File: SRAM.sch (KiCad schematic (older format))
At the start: 12 parts

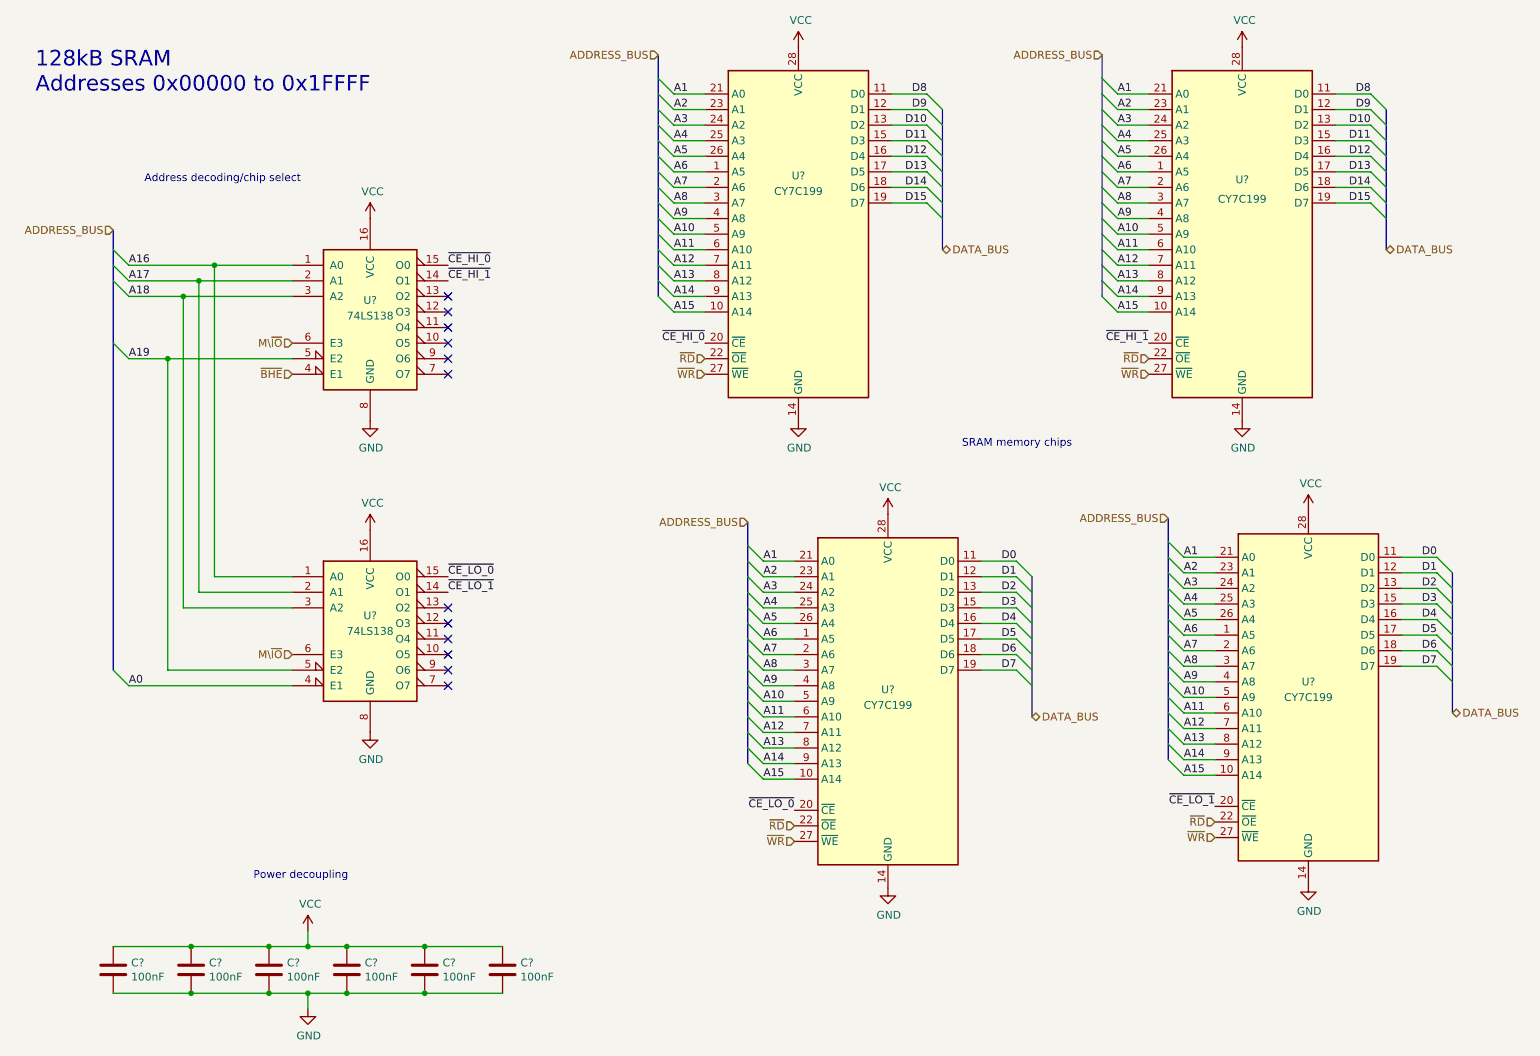
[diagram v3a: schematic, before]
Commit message: Updates to pass ERC
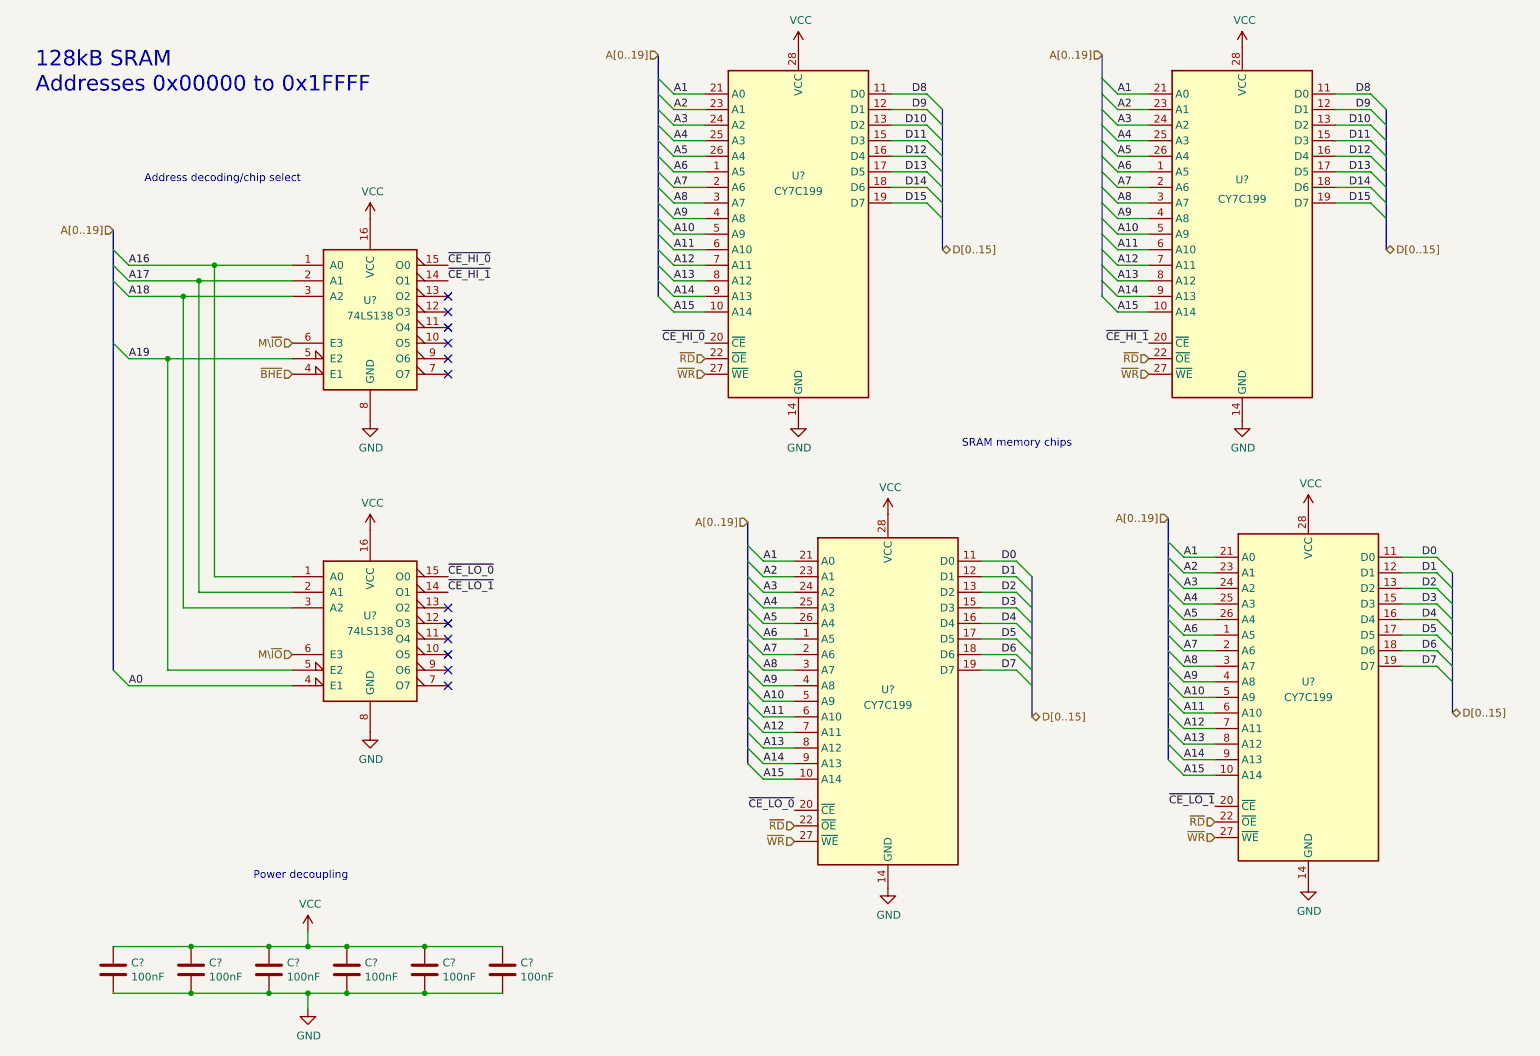
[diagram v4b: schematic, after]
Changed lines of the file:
@@
 	5050 1825 4850 1825
 Text HLabel 4750 875  0    50   Input ~ 0
-ADDRESS_BUS
+A[0..19]
 Wire Wire Line
 	7900 2525 7700 2525
@@
 	7900 1825 7700 1825
 Text HLabel 7600 875  0    50   Input ~ 0
-ADDRESS_BUS
+A[0..19]
 Wire Wire Line
 	5625 5525 5425 5525
@@
 	5625 4825 5425 4825
 Text HLabel 5325 3875 0    50   Input ~ 0
-ADDRESS_BUS
+A[0..19]
 Wire Wire Line
 	8325 5500 8125 5500
@@
 	8325 4800 8125 4800
 Text HLabel 8025 3850 0    50   Input ~ 0
-ADDRESS_BUS
+A[0..19]
 Entry Wire Line
 	7600 2425 7700 2525
@@
 $EndComp
 Text HLabel 1250 2000 0    50   Input ~ 0
-ADDRESS_BUS
+A[0..19]
 Entry Wire Line
 	1250 4825 1350 4925
@@
 	6575 1825 6475 1725
 Text HLabel 6575 2125 2    50   BiDi ~ 0
-DATA_BUS
+D[0..15]
 Wire Wire Line
 	9100 1825 9325 1825
@@
 	9425 1825 9325 1725
 Text HLabel 9425 2125 2    50   BiDi ~ 0
-DATA_BUS
+D[0..15]
 Wire Wire Line
 	9525 4800 9750 4800
@@
 	9850 4800 9750 4700
 Text HLabel 9850 5100 2    50   BiDi ~ 0
-DATA_BUS
+D[0..15]
 Wire Wire Line
 	6825 4825 7050 4825
@@
 	7150 4825 7050 4725
 Text HLabel 7150 5125 2    50   BiDi ~ 0
-DATA_BUS
+D[0..15]
 Wire Wire Line
 	1350 4925 2400 4925

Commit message: Assign footprints for most symbols
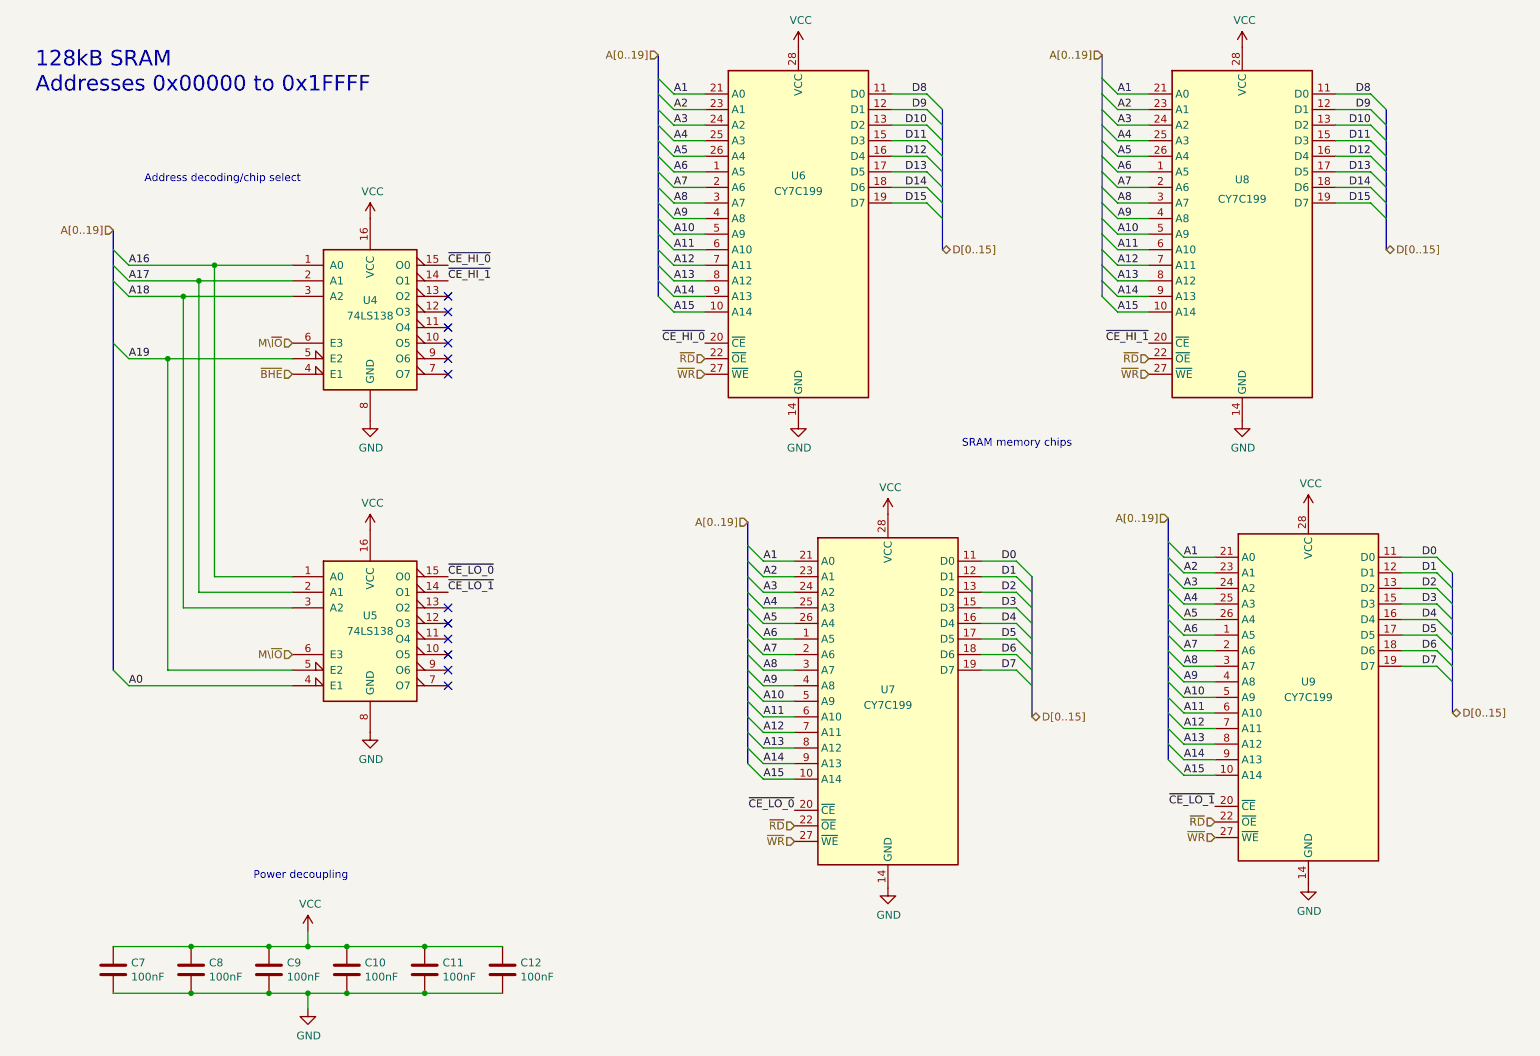
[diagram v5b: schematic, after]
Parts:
- C10, C11, C12, C7, C8, C9: renamed from C?; footprint (none) -> Capacitor_THT:C_Rect_L4.0mm_W2.5mm_P2.50mm
- U4, U5: renamed from U?; footprint (none) -> Package_DIP:DIP-16_W7.62mm
- U6, U7, U8, U9: renamed from U?; footprint (none) -> Package_DIP:DIP-28_W7.62mm
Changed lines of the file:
@@
 $EndDescr
 $Comp
-L Memory_RAM:CY7C199 U?
+L Memory_RAM:CY7C199 U6
 U 1 1 61AAD851
 P 5650 2025
-F 0 "U?" H 5650 2400 50  0000 C CNN
+F 0 "U6" H 5650 2400 50  0000 C CNN
 F 1 "CY7C199" H 5650 2300 50  0000 C CNN
-F 2 "" H 5650 2025 50  0001 C CNN
+F 2 "Package_DIP:DIP-28_W7.62mm" H 5650 2025 50  0001 C CNN
 F 3 "" H 5650 2025 50  0001 C CNN
 	1    5650 2025
@@
 $EndComp
 $Comp
-L Memory_RAM:CY7C199 U?
+L Memory_RAM:CY7C199 U8
 U 1 1 61AB54DC
 P 8500 2025
-F 0 "U?" H 8500 2375 50  0000 C CNN
+F 0 "U8" H 8500 2375 50  0000 C CNN
 F 1 "CY7C199" H 8500 2250 50  0000 C CNN
-F 2 "" H 8500 2025 50  0001 C CNN
+F 2 "Package_DIP:DIP-28_W7.62mm" H 8500 2025 50  0001 C CNN
 F 3 "" H 8500 2025 50  0001 C CNN
 	1    8500 2025
@@
 $EndComp
 $Comp
-L Memory_RAM:CY7C199 U?
+L Memory_RAM:CY7C199 U7
 U 1 1 61AB671A
 P 6225 5025
-F 0 "U?" H 6225 5100 50  0000 C CNN
+F 0 "U7" H 6225 5100 50  0000 C CNN
 F 1 "CY7C199" H 6225 5000 50  0000 C CNN
-F 2 "" H 6225 5025 50  0001 C CNN
+F 2 "Package_DIP:DIP-28_W7.62mm" H 6225 5025 50  0001 C CNN
 F 3 "" H 6225 5025 50  0001 C CNN
 	1    6225 5025
@@
 $EndComp
 $Comp
-L Memory_RAM:CY7C199 U?
+L Memory_RAM:CY7C199 U9
 U 1 1 61AB67E4
 P 8925 5000
-F 0 "U?" H 8925 5100 50  0000 C CNN
+F 0 "U9" H 8925 5100 50  0000 C CNN
 F 1 "CY7C199" H 8925 5000 50  0000 C CNN
-F 2 "" H 8925 5000 50  0001 C CNN
+F 2 "Package_DIP:DIP-28_W7.62mm" H 8925 5000 50  0001 C CNN
 F 3 "" H 8925 5000 50  0001 C CNN
 	1    8925 5000
@@
 $EndComp
 $Comp
-L power:VCC #PWR?
+L power:VCC #PWR0119
 U 1 1 61AC733D
 P 5650 825
-F 0 "#PWR?" H 5650 675 50  0001 C CNN
+F 0 "#PWR0119" H 5650 675 50  0001 C CNN
 F 1 "VCC" H 5665 998 50  0000 C CNN
 F 2 "" H 5650 825 50  0001 C CNN
@@
 $EndComp
 $Comp
-L power:VCC #PWR?
+L power:VCC #PWR0121
 U 1 1 61ACC468
 P 8500 825
-F 0 "#PWR?" H 8500 675 50  0001 C CNN
+F 0 "#PWR0121" H 8500 675 50  0001 C CNN
 F 1 "VCC" H 8515 998 50  0000 C CNN
 F 2 "" H 8500 825 50  0001 C CNN
@@
 $EndComp
 $Comp
-L power:VCC #PWR?
+L power:VCC #PWR0127
 U 1 1 61AD1B1E
 P 6225 3825
-F 0 "#PWR?" H 6225 3675 50  0001 C CNN
+F 0 "#PWR0127" H 6225 3675 50  0001 C CNN
 F 1 "VCC" H 6240 3998 50  0000 C CNN
 F 2 "" H 6225 3825 50  0001 C CNN
@@
 $EndComp
 $Comp
-L power:VCC #PWR?
+L power:VCC #PWR0128
 U 1 1 61AD20F7
 P 8925 3800
-F 0 "#PWR?" H 8925 3650 50  0001 C CNN
+F 0 "#PWR0128" H 8925 3650 50  0001 C CNN
 F 1 "VCC" H 8940 3973 50  0000 C CNN
 F 2 "" H 8925 3800 50  0001 C CNN
@@
 $EndComp
 $Comp
-L power:GND #PWR?
+L power:GND #PWR0129
 U 1 1 61AD3257
 P 5650 3225
-F 0 "#PWR?" H 5650 2975 50  0001 C CNN
+F 0 "#PWR0129" H 5650 2975 50  0001 C CNN
 F 1 "GND" H 5655 3052 50  0000 C CNN
 F 2 "" H 5650 3225 50  0001 C CNN
@@
 $EndComp
 $Comp
-L power:GND #PWR?
+L power:GND #PWR0130
 U 1 1 61AD38A8
 P 8500 3225
-F 0 "#PWR?" H 8500 2975 50  0001 C CNN
+F 0 "#PWR0130" H 8500 2975 50  0001 C CNN
 F 1 "GND" H 8505 3052 50  0000 C CNN
 F 2 "" H 8500 3225 50  0001 C CNN
@@
 $EndComp
 $Comp
-L power:GND #PWR?
+L power:GND #PWR0131
 U 1 1 61AD46AD
 P 6225 6225
-F 0 "#PWR?" H 6225 5975 50  0001 C CNN
+F 0 "#PWR0131" H 6225 5975 50  0001 C CNN
 F 1 "GND" H 6230 6052 50  0000 C CNN
 F 2 "" H 6225 6225 50  0001 C CNN
@@
 $EndComp
 $Comp
-L power:GND #PWR?
+L power:GND #PWR0132
 U 1 1 61AD51C3
 P 8925 6200
-F 0 "#PWR?" H 8925 5950 50  0001 C CNN
+F 0 "#PWR0132" H 8925 5950 50  0001 C CNN
 F 1 "GND" H 8930 6027 50  0000 C CNN
 F 2 "" H 8925 6200 50  0001 C CNN
@@
 	7600 2425 7700 2525
 $Comp
-L power:GND #PWR?
+L power:GND #PWR0133
 U 1 1 61B73702
 P 2900 5225
-F 0 "#PWR?" H 2900 4975 50  0001 C CNN
+F 0 "#PWR0133" H 2900 4975 50  0001 C CNN
 F 1 "GND" H 2905 5052 50  0000 C CNN
 F 2 "" H 2900 5225 50  0001 C CNN
@@
 $EndComp
 $Comp
-L power:VCC #PWR?
+L power:VCC #PWR0134
 U 1 1 61B71B7C
 P 2900 3925
-F 0 "#PWR?" H 2900 3775 50  0001 C CNN
+F 0 "#PWR0134" H 2900 3775 50  0001 C CNN
 F 1 "VCC" H 2915 4098 50  0000 C CNN
 F 2 "" H 2900 3925 50  0001 C CNN
@@
 $EndComp
 $Comp
-L 74xx:74LS138 U?
+L 74xx:74LS138 U5
 U 1 1 61ADBC92
 P 2900 4525
-F 0 "U?" H 2900 4575 50  0000 C CNN
+F 0 "U5" H 2900 4575 50  0000 C CNN
 F 1 "74LS138" H 2900 4475 50  0000 C CNN
-F 2 "" H 2900 4525 50  0001 C CNN
+F 2 "Package_DIP:DIP-16_W7.62mm" H 2900 4525 50  0001 C CNN
 F 3 "http://www.ti.com/lit/gpn/sn74LS138" H 2900 4525 50  0001 C CNN
 	1    2900 4525
@@
 $EndComp
 $Comp
-L power:GND #PWR?
+L power:GND #PWR0135
 U 1 1 61B73092
 P 2900 3225
-F 0 "#PWR?" H 2900 2975 50  0001 C CNN
+F 0 "#PWR0135" H 2900 2975 50  0001 C CNN
 F 1 "GND" H 2905 3052 50  0000 C CNN
 F 2 "" H 2900 3225 50  0001 C CNN
@@
 $EndComp
 $Comp
-L power:VCC #PWR?
+L power:VCC #PWR0136
 U 1 1 61B71456
 P 2900 1925
-F 0 "#PWR?" H 2900 1775 50  0001 C CNN
+F 0 "#PWR0136" H 2900 1775 50  0001 C CNN
 F 1 "VCC" H 2915 2098 50  0000 C CNN
 F 2 "" H 2900 1925 50  0001 C CNN
@@
 $EndComp
 $Comp
-L 74xx:74LS138 U?
+L 74xx:74LS138 U4
 U 1 1 61AD932E
 P 2900 2525
-F 0 "U?" H 2900 2600 50  0000 C CNN
+F 0 "U4" H 2900 2600 50  0000 C CNN
 F 1 "74LS138" H 2900 2500 50  0000 C CNN
-F 2 "" H 2900 2525 50  0001 C CNN
+F 2 "Package_DIP:DIP-16_W7.62mm" H 2900 2525 50  0001 C CNN
 F 3 "http://www.ti.com/lit/gpn/sn74LS138" H 2900 2525 50  0001 C CNN
 	1    2900 2525
@@
 	1350 4925 2400 4925
 $Comp
-L Device:C C?
+L Device:C C7
 U 1 1 61AB8F40
 P 1250 6750
-F 0 "C?" H 1365 6796 50  0000 L CNN
+F 0 "C7" H 1365 6796 50  0000 L CNN
 F 1 "100nF" H 1365 6705 50  0000 L CNN
-F 2 "" H 1288 6600 50  0001 C CNN
+F 2 "Capacitor_THT:C_Rect_L4.0mm_W2.5mm_P2.50mm" H 1288 6600 50  0001 C CNN
 F 3 "~" H 1250 6750 50  0001 C CNN
 	1    1250 6750
@@
 $EndComp
 $Comp
-L Device:C C?
+L Device:C C8
 U 1 1 61AF79B9
 P 1750 6750
-F 0 "C?" H 1865 6796 50  0000 L CNN
+F 0 "C8" H 1865 6796 50  0000 L CNN
 F 1 "100nF" H 1865 6705 50  0000 L CNN
-F 2 "" H 1788 6600 50  0001 C CNN
+F 2 "Capacitor_THT:C_Rect_L4.0mm_W2.5mm_P2.50mm" H 1788 6600 50  0001 C CNN
 F 3 "~" H 1750 6750 50  0001 C CNN
 	1    1750 6750
@@
 $EndComp
 $Comp
-L Device:C C?
+L Device:C C9
 U 1 1 61AF7D5B
 P 2250 6750
-F 0 "C?" H 2365 6796 50  0000 L CNN
+F 0 "C9" H 2365 6796 50  0000 L CNN
 F 1 "100nF" H 2365 6705 50  0000 L CNN
-F 2 "" H 2288 6600 50  0001 C CNN
+F 2 "Capacitor_THT:C_Rect_L4.0mm_W2.5mm_P2.50mm" H 2288 6600 50  0001 C CNN
 F 3 "~" H 2250 6750 50  0001 C CNN
 	1    2250 6750
@@
 $EndComp
 $Comp
-L Device:C C?
+L Device:C C10
 U 1 1 61B07796
 P 2750 6750
-F 0 "C?" H 2865 6796 50  0000 L CNN
+F 0 "C10" H 2865 6796 50  0000 L CNN
 F 1 "100nF" H 2865 6705 50  0000 L CNN
-F 2 "" H 2788 6600 50  0001 C CNN
+F 2 "Capacitor_THT:C_Rect_L4.0mm_W2.5mm_P2.50mm" H 2788 6600 50  0001 C CNN
 F 3 "~" H 2750 6750 50  0001 C CNN
 	1    2750 6750
@@
 $EndComp
 $Comp
-L Device:C C?
+L Device:C C11
 U 1 1 61B07808
 P 3250 6750
-F 0 "C?" H 3365 6796 50  0000 L CNN
+F 0 "C11" H 3365 6796 50  0000 L CNN
 F 1 "100nF" H 3365 6705 50  0000 L CNN
-F 2 "" H 3288 6600 50  0001 C CNN
+F 2 "Capacitor_THT:C_Rect_L4.0mm_W2.5mm_P2.50mm" H 3288 6600 50  0001 C CNN
 F 3 "~" H 3250 6750 50  0001 C CNN
 	1    3250 6750
@@
 $EndComp
 $Comp
-L Device:C C?
+L Device:C C12
 U 1 1 61B07812
 P 3750 6750
-F 0 "C?" H 3865 6796 50  0000 L CNN
+F 0 "C12" H 3865 6796 50  0000 L CNN
 F 1 "100nF" H 3865 6705 50  0000 L CNN
-F 2 "" H 3788 6600 50  0001 C CNN
+F 2 "Capacitor_THT:C_Rect_L4.0mm_W2.5mm_P2.50mm" H 3788 6600 50  0001 C CNN
 F 3 "~" H 3750 6750 50  0001 C CNN
 	1    3750 6750
@@
 $EndComp
 $Comp
-L power:VCC #PWR?
+L power:VCC #PWR0137
 U 1 1 61B1039C
 P 2500 6500
-F 0 "#PWR?" H 2500 6350 50  0001 C CNN
+F 0 "#PWR0137" H 2500 6350 50  0001 C CNN
 F 1 "VCC" H 2515 6673 50  0000 C CNN
 F 2 "" H 2500 6500 50  0001 C CNN
@@
 $EndComp
 $Comp
-L power:GND #PWR?
+L power:GND #PWR0138
 U 1 1 61B10828
 P 2500 7000
-F 0 "#PWR?" H 2500 6750 50  0001 C CNN
+F 0 "#PWR0138" H 2500 6750 50  0001 C CNN
 F 1 "GND" H 2505 6827 50  0000 C CNN
 F 2 "" H 2500 7000 50  0001 C CNN
